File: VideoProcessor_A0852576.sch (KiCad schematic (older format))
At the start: 0 parts

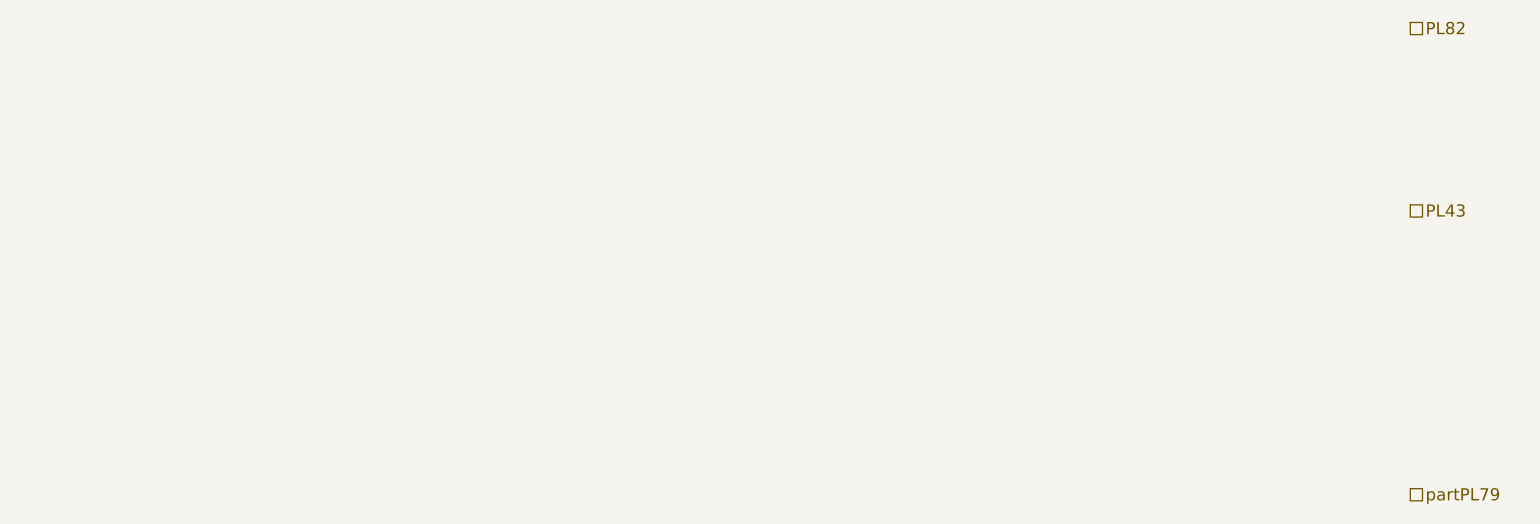
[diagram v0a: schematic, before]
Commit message: Adds Video Processor PCB
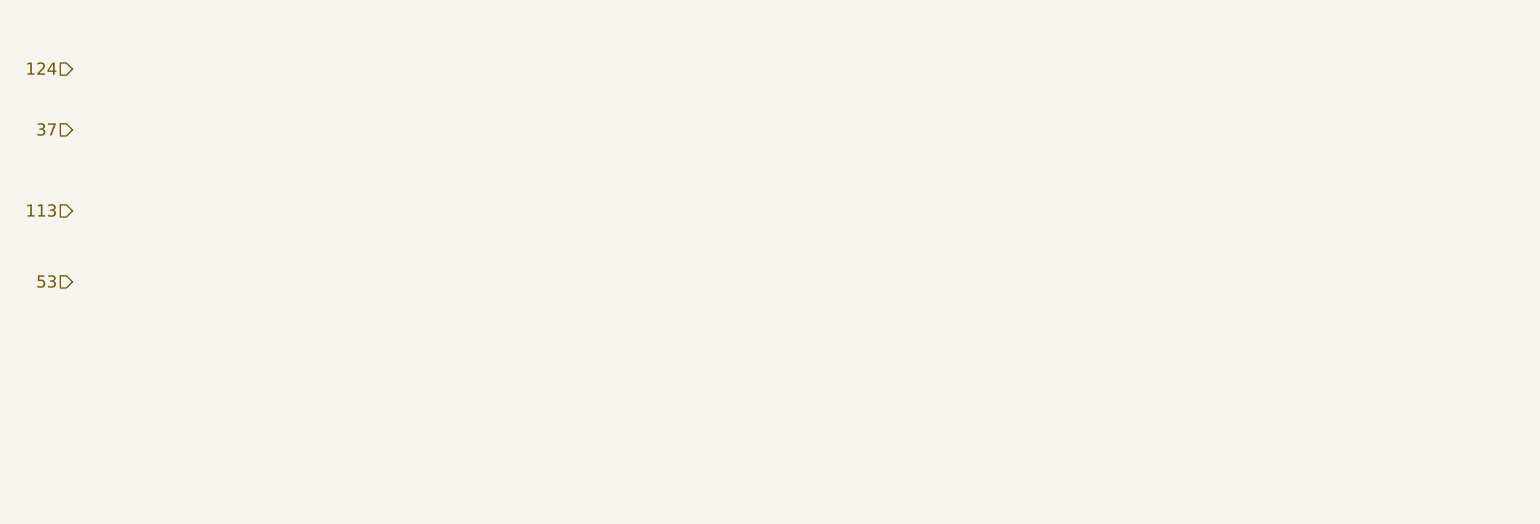
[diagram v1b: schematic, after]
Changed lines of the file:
@@
 $Descr A4 11693 8268
 encoding utf-8
-Sheet 10 16
+Sheet 16 16
 Title ""
 Date ""
@@
 Comment4 ""
 $EndDescr
-Text HLabel 8900 1600 2    60   UnSpc ~ 0
-PL82
-Text HLabel 8900 2500 2    60   UnSpc ~ 0
-PL43
-Text HLabel 8900 3900 2    60   UnSpc ~ 0
-partPL79
+Text HLabel 2300 1800 0    60   Input ~ 0
+124
+Text HLabel 2300 2100 0    60   Input ~ 0
+37
+Text HLabel 2300 2500 0    60   Input ~ 0
+113
+Text HLabel 2300 2850 0    60   Input ~ 0
+53
 $EndSCHEMATC
